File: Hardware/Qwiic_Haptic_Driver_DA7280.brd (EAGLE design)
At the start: 25.4 x 25.4 mm, 48 parts, among them J1 QWIIC_RIGHT_ANGLE, J2 QWIIC_RIGHT_ANGLE, M1 G1040003D_COIN_VIBRATION_MOTOR, U1 HAPTIC_DRIVER_DA7280

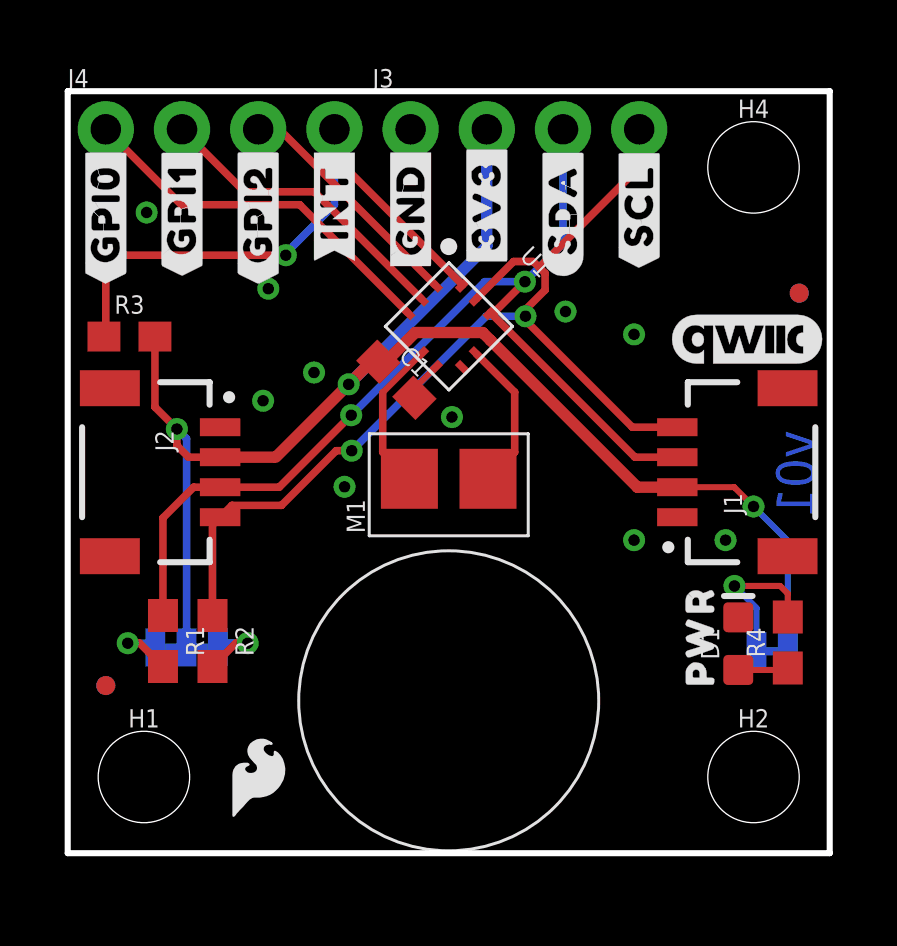
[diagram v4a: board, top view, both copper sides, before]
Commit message: Adds new package for the vibration motor - one that will go through the PCB
* The new package has castellated leads to the part was rotated 180 degrees to the edge of the board.
* Fixes interrupt silk to reflect active low
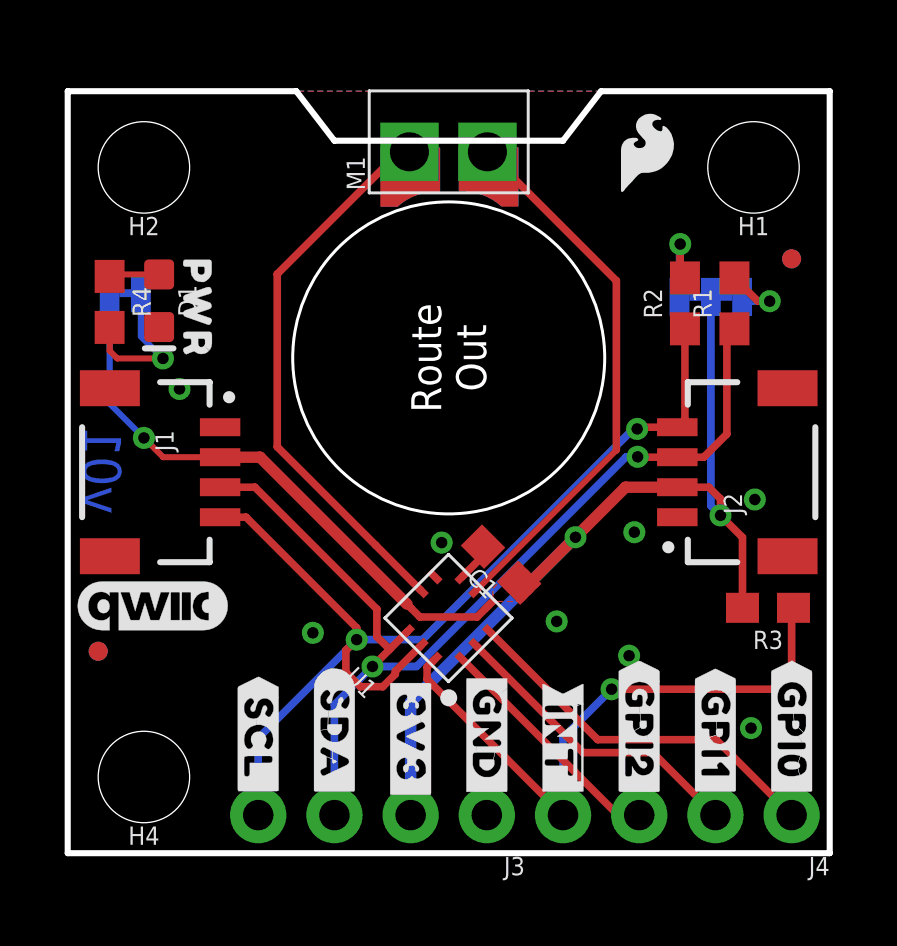
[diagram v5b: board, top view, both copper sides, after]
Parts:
- removed LOGO1: SFE_LOGO_NAME_FLAME.1_INCH, SparkFun-Aesthetics:SFE_LOGO_NAME_FLAME_.1
- removed U$15: (no value), bot:#INT#3
- removed U$7: (no value), top:#INT#6
- added U$26: (no value), SparkFun-Aesthetics:SFE_LOGO_FLAME_.1
- added U$27: (no value), bot:##INT##3
- added U$28: (no value), top:##INT##6
- M1: value G1040003D_COIN_VIBRATION_MOTOR -> G1040003D_LRA_CASTELLATED; device TEMP:COIN_VIBRATION_MOTOR -> TEMP:COIN_VIBRATION_MOTOR_CASTEL
- moved J4 32.3 mm to (24.1, 1.27), turned to 180 degrees
- moved H1 28.7 mm to (22.9, 22.9), turned to 180 degrees
- moved H2 28.7 mm to (2.54, 22.9), turned to 180 degrees
- moved H4 28.7 mm to (2.54, 2.54), turned to 180 degrees
- moved U$4 28.7 mm to (24.1, 4.06), turned to 270 degrees
- moved FD3 26.9 mm to (24.1, 19.8), turned to 180 degrees
- moved FD4 26.9 mm to (24.1, 19.8), turned to 180 degrees
- moved FD1 26.2 mm to (1.02, 6.73), turned to 180 degrees
- moved FD2 26.2 mm to (1.02, 6.73), turned to 180 degrees
- moved U$12 26.2 mm to (24.1, 6.30), turned to 90 degrees
- moved R4 25.3 mm to (1.40, 18.4), turned to 270 degrees
- moved U$13 25.0 mm to (21.6, 3.94), turned to 90 degrees
- moved U$5 25.0 mm to (21.6, 3.94), turned to 270 degrees
- moved JP1 24.6 mm to (1.92, 18.7), turned to 0 degrees
- moved U$17 24.5 mm to (19.3, 23.4)
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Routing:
- net N$5: track 5.06 -> 18.6 mm
- net N$6: track 5.06 -> 18.3 mm
- net SCL: track 33.7 -> 35.2 mm
- net GND: vias 10 -> 8
- added copper zone on layer 1, net 3.3V
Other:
- outline, holes or cut-outs redrawn
